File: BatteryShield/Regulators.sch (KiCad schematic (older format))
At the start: 14 parts

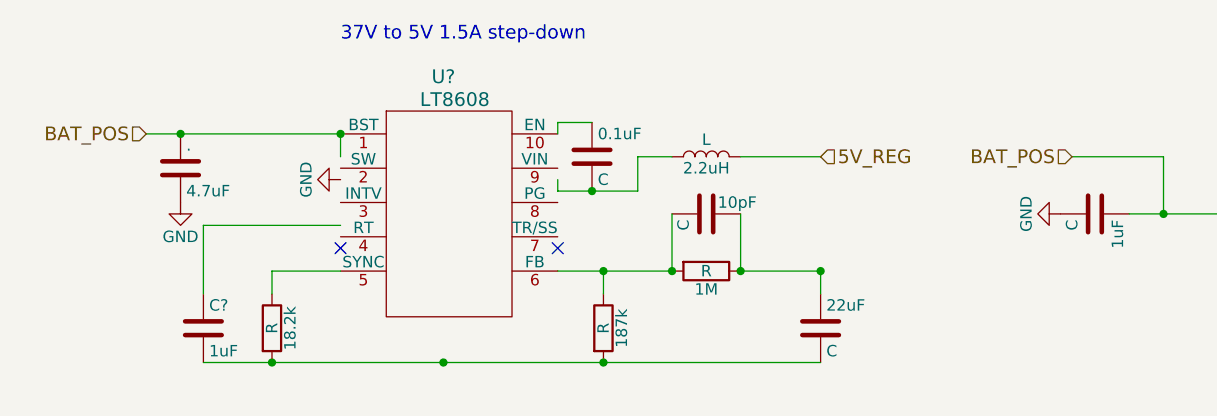
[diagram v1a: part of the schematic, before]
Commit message: Added two pages, cleaned up net names
Cleaned up net names. Added protection/grounding and BBB interface socket. Additional work needs to be done with grounding/mounting holes and 37V rail reverse current protection.
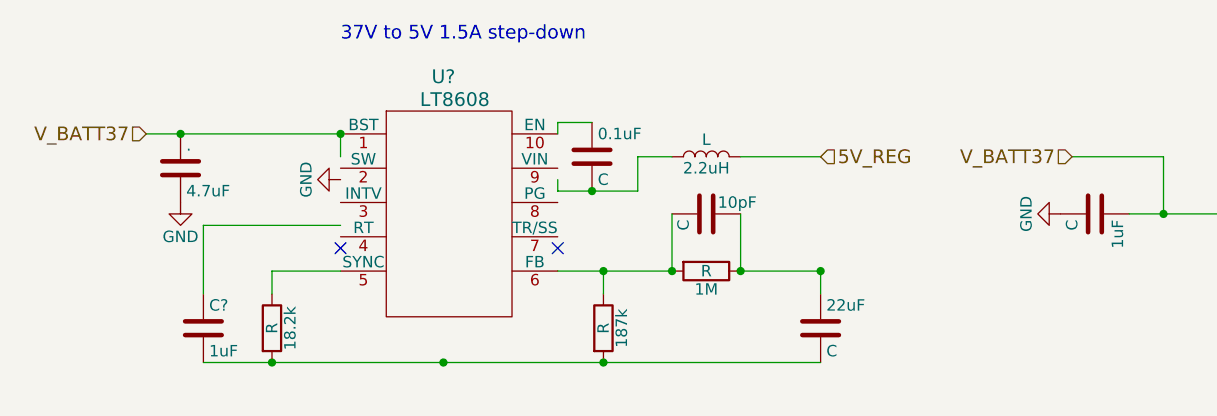
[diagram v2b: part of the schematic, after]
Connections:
- net labels added: V_BATT37
- net labels removed: BAT_POS
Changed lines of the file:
@@
 $Descr A4 11693 8268
 encoding utf-8
-Sheet 9 10
+Sheet 9 12
 Title ""
 Date ""
@@
 37V to 5V 1.5A step-down
 Text HLabel 1600 3050 0    60   Input ~ 0
-BAT_POS
+V_BATT37
 $Comp
 L C .
@@
 	5900 3400 6500 3400
 Text HLabel 5650 3150 0    60   Input ~ 0
-BAT_POS
+V_BATT37
 Wire Wire Line
 	5650 3150 6050 3150

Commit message: Associated a lot of footprints
Now I need to add a lot more :(
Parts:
- U?: footprint (none) -> footprints:MSOP10
- U?: footprint (none) -> footprints:MSOP8
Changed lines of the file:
@@
 $Descr A4 11693 8268
 encoding utf-8
-Sheet 9 12
+Sheet 12 12
 Title ""
 Date ""
@@
 F 0 "U?" H 2900 3900 60  0000 C CNN
 F 1 "LT8608" H 2950 3800 60  0000 C CNN
-F 2 "" H 2900 3350 60  0001 C CNN
-F 3 "" H 2900 3350 60  0001 C CNN
+F 2 "footprints:MSOP10" H 2900 3350 60  0001 C CNN
+F 3 "http://www.analog.com/media/en/technical-documentation/data-sheets/lt8608.pdf" H 2900 3350 60  0001 C CNN
 	1    2900 3350
 	1    0    0    -1
@@
 F 0 "U?" H 7000 3700 60  0000 C CNN
 F 1 "LTC3642-3.3" H 7000 3600 60  0000 C CNN
-F 2 "" H 6950 3350 60  0001 C CNN
-F 3 "" H 6950 3350 60  0001 C CNN
+F 2 "footprints:MSOP8" H 6950 3350 60  0001 C CNN
+F 3 "http://www.analog.com/media/en/technical-documentation/data-sheets/3642fc.pdf?domain=www.linear.com" H 6950 3350 60  0001 C CNN
 	1    6950 3350
 	1    0    0    -1

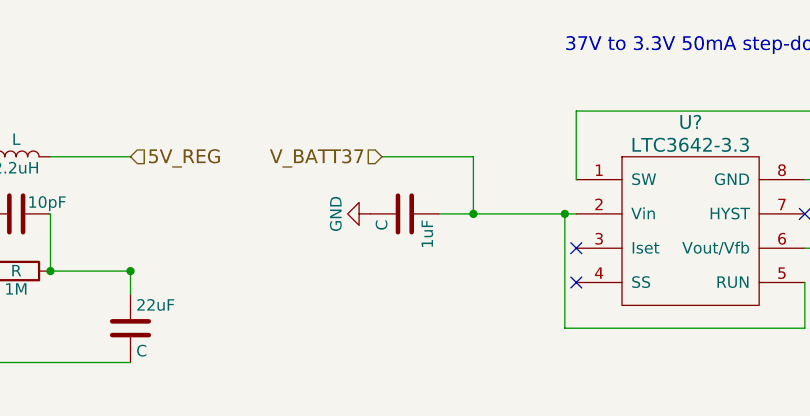
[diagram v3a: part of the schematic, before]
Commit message: Added more footprints
wow. much many foot prints
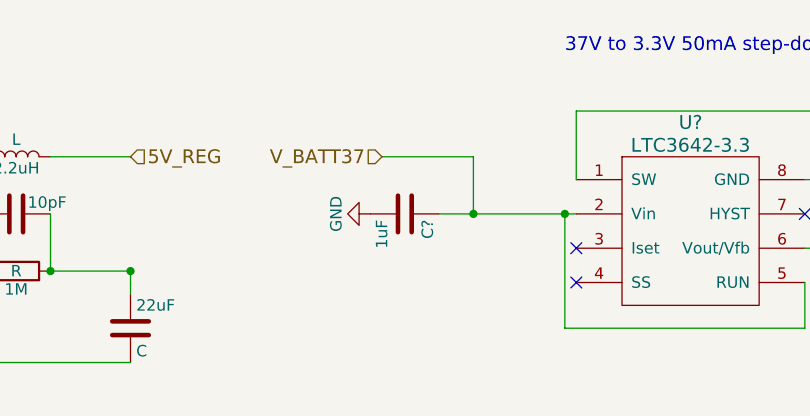
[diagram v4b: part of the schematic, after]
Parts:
- removed 1uF: C, symbol C
- added C?: 1uF, Capacitors_SMD:C_0603, symbol C
- ., 10pF, C?: footprint (none) -> Capacitors_SMD:C_0603
- 0.1uF: footprint (none) -> Capacitors_SMD:C_0402
- 10uF, 22uF: footprint (none) -> Capacitors_SMD:C_0805
- 150uH: footprint (none) -> Inductors_SMD:L_Wuerth_HCI-1350
- 18.2k: footprint (none) -> Resistors_SMD:R_0603
- 187k, 1M: footprint (none) -> Resistors_SMD:R_0805
- 2.2uH: footprint (none) -> Inductors_SMD:L_1812
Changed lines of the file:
@@
 F 0 "." H 1775 3300 50  0000 L CNN
 F 1 "4.7uF" H 1775 3100 50  0000 L CNN
-F 2 "" H 1788 3050 50  0001 C CNN
-F 3 "" H 1750 3200 50  0001 C CNN
+F 2 "Capacitors_SMD:C_0603" H 1788 3050 50  0001 C CNN
+F 3 "http://www.samsungsem.com/kr/support/product-search/mlcc/__icsFiles/afieldfile/2017/10/14/Spec%20sheet_CL10B475KQ8NQNC.pdf" H 1750 3200 50  0001 C CNN
 	1    1750 3200
 	1    0    0    -1
@@
 F 0 "C?" H 1875 4000 50  0000 L CNN
 F 1 "1uF" H 1875 3800 50  0000 L CNN
-F 2 "" H 1888 3750 50  0001 C CNN
-F 3 "" H 1850 3900 50  0001 C CNN
+F 2 "Capacitors_SMD:C_0603" H 1888 3750 50  0001 C CNN
+F 3 "http://www.samsungsem.com/kr/support/product-search/mlcc/__icsFiles/afieldfile/2017/07/27/Spec%20sheet_CL10B105MO8NNWC.pdf" H 1850 3900 50  0001 C CNN
 	1    1850 3900
 	1    0    0    -1
@@
 F 0 "18.2k" V 2230 3900 50  0000 C CNN
 F 1 "R" V 2150 3900 50  0000 C CNN
-F 2 "" V 2080 3900 50  0001 C CNN
-F 3 "" H 2150 3900 50  0001 C CNN
+F 2 "Resistors_SMD:R_0603" V 2080 3900 50  0001 C CNN
+F 3 "https://industrial.panasonic.com/cdbs/www-data/pdf/RDM0000/AOA0000C307.pdf" H 2150 3900 50  0001 C CNN
 	1    2150 3900
 	1    0    0    -1
@@
 F 0 "187k" V 3680 3900 50  0000 C CNN
 F 1 "R" V 3600 3900 50  0000 C CNN
-F 2 "" V 3530 3900 50  0001 C CNN
-F 3 "" H 3600 3900 50  0001 C CNN
+F 2 "Resistors_SMD:R_0805" V 3530 3900 50  0001 C CNN
+F 3 "https://www.digikey.ca/product-detail/en/panasonic-electronic-components/ERA-6AEB1873V/P187KDACT-ND/3075001" H 3600 3900 50  0001 C CNN
 	1    3600 3900
 	1    0    0    -1
@@
 F 0 "10pF" V 4000 3450 50  0000 L CNN
 F 1 "C" H 4075 3300 50  0000 L CNN
-F 2 "" H 4088 3250 50  0001 C CNN
-F 3 "" H 4050 3400 50  0001 C CNN
+F 2 "Capacitors_SMD:C_0603" H 4088 3250 50  0001 C CNN
+F 3 "https://www.murata.com/~/media/webrenewal/support/library/catalog/products/capacitor/mlcc/c02e.ashx" H 4050 3400 50  0001 C CNN
 	1    4050 3400
 	0    1    1    0
@@
 F 0 "1M" V 4130 3650 50  0000 C CNN
 F 1 "R" V 4050 3650 50  0000 C CNN
-F 2 "" V 3980 3650 50  0001 C CNN
-F 3 "" H 4050 3650 50  0001 C CNN
+F 2 "Resistors_SMD:R_0805" V 3980 3650 50  0001 C CNN
+F 3 "https://industrial.panasonic.com/cdbs/www-data/pdf/RDM0000/AOA0000C307.pdf" H 4050 3650 50  0001 C CNN
 	1    4050 3650
 	0    1    1    0
@@
 F 0 "22uF" H 4575 4000 50  0000 L CNN
 F 1 "C" H 4575 3800 50  0000 L CNN
-F 2 "" H 4588 3750 50  0001 C CNN
-F 3 "" H 4550 3900 50  0001 C CNN
+F 2 "Capacitors_SMD:C_0805" H 4588 3750 50  0001 C CNN
+F 3 "http://www.samsungsem.com/kr/support/product-search/mlcc/__icsFiles/afieldfile/2017/07/28/S_CL21A226MOCLRNC.pdf" H 4550 3900 50  0001 C CNN
 	1    4550 3900
 	1    0    0    -1
@@
 F 0 "0.1uF" H 3575 3250 50  0000 L CNN
 F 1 "C" H 3575 3050 50  0000 L CNN
-F 2 "" H 3588 3000 50  0001 C CNN
-F 3 "" H 3550 3150 50  0001 C CNN
+F 2 "Capacitors_SMD:C_0402" H 3588 3000 50  0001 C CNN
+F 3 "http://www.samsungsem.com/kr/support/product-search/mlcc/__icsFiles/afieldfile/2016/08/18/S_CL05F104ZO5NNNC.pdf" H 3550 3150 50  0001 C CNN
 	1    3550 3150
 	1    0    0    -1
@@
 F 0 "2.2uH" V 4000 3150 50  0000 C CNN
 F 1 "L" V 4125 3150 50  0000 C CNN
-F 2 "" H 4050 3150 50  0001 C CNN
-F 3 "" H 4050 3150 50  0001 C CNN
+F 2 "Inductors_SMD:L_1812" H 4050 3150 50  0001 C CNN
+F 3 "http://www.vishay.com/docs/34061/isc1812.pdf" H 4050 3150 50  0001 C CNN
 	1    4050 3150
 	0    -1   -1   0
@@
 	6050 3150 6050 3400
 Connection ~ 6450 3400
-$Comp
-L C 1uF
-U 1 1 5A920FC1
-P 5750 3400
-F 0 "1uF" H 5775 3500 50  0000 L CNN
-F 1 "C" H 5775 3300 50  0000 L CNN
-F 2 "" H 5788 3250 50  0001 C CNN
-F 3 "" H 5750 3400 50  0001 C CNN
-	1    5750 3400
-	0    1    1    0
-$EndComp
 Connection ~ 6050 3400
 $Comp
@@
 F 0 "150uH" V 8050 3250 50  0000 C CNN
 F 1 "L" V 8175 3250 50  0000 C CNN
-F 2 "" H 8100 3250 50  0001 C CNN
-F 3 "" H 8100 3250 50  0001 C CNN
+F 2 "Inductors_SMD:L_Wuerth_HCI-1350" H 8100 3250 50  0001 C CNN
+F 3 "http://katalog.we-online.de/pbs/datasheet/7447709151.pdf" H 8100 3250 50  0001 C CNN
 	1    8100 3250
 	1    0    0    -1
@@
 F 0 "10uF" H 8275 3950 50  0000 L CNN
 F 1 "C" H 8275 3750 50  0000 L CNN
-F 2 "" H 8288 3700 50  0001 C CNN
-F 3 "" H 8250 3850 50  0001 C CNN
+F 2 "Capacitors_SMD:C_0805" H 8288 3700 50  0001 C CNN
+F 3 "http://www.samsungsem.com/kr/support/product-search/mlcc/CL21A106KPCLQNC.jsp" H 8250 3850 50  0001 C CNN
 	1    8250 3850
 	1    0    0    -1
@@
 	1    0    0    -1
 $EndComp
+$Comp
+L C C?
+U 1 1 5B29BC47
+P 5750 3400
+F 0 "C?" H 5775 3500 50  0000 L CNN
+F 1 "1uF" H 5775 3300 50  0000 L CNN
+F 2 "Capacitors_SMD:C_0603" H 5788 3250 50  0001 C CNN
+F 3 "http://www.samsungsem.com/kr/support/product-search/mlcc/__icsFiles/afieldfile/2017/07/27/Spec%20sheet_CL10B105MO8NNWC.pdf" H 5750 3400 50  0001 C CNN
+	1    5750 3400
+	0    1    1    0
+$EndComp
 $EndSCHEMATC

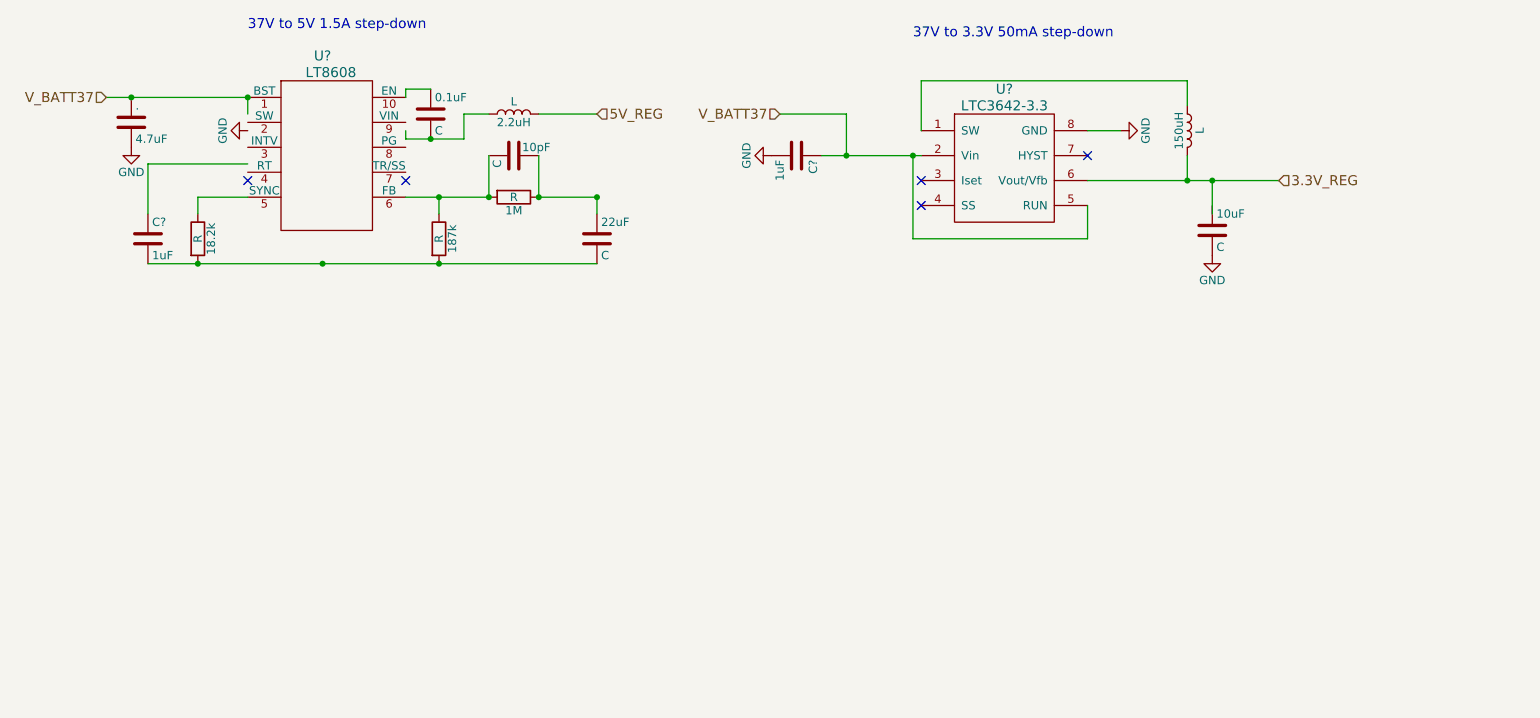
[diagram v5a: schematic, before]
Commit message: Did V.1 of layout; removed old circuits
gosh I need to do schoolwork
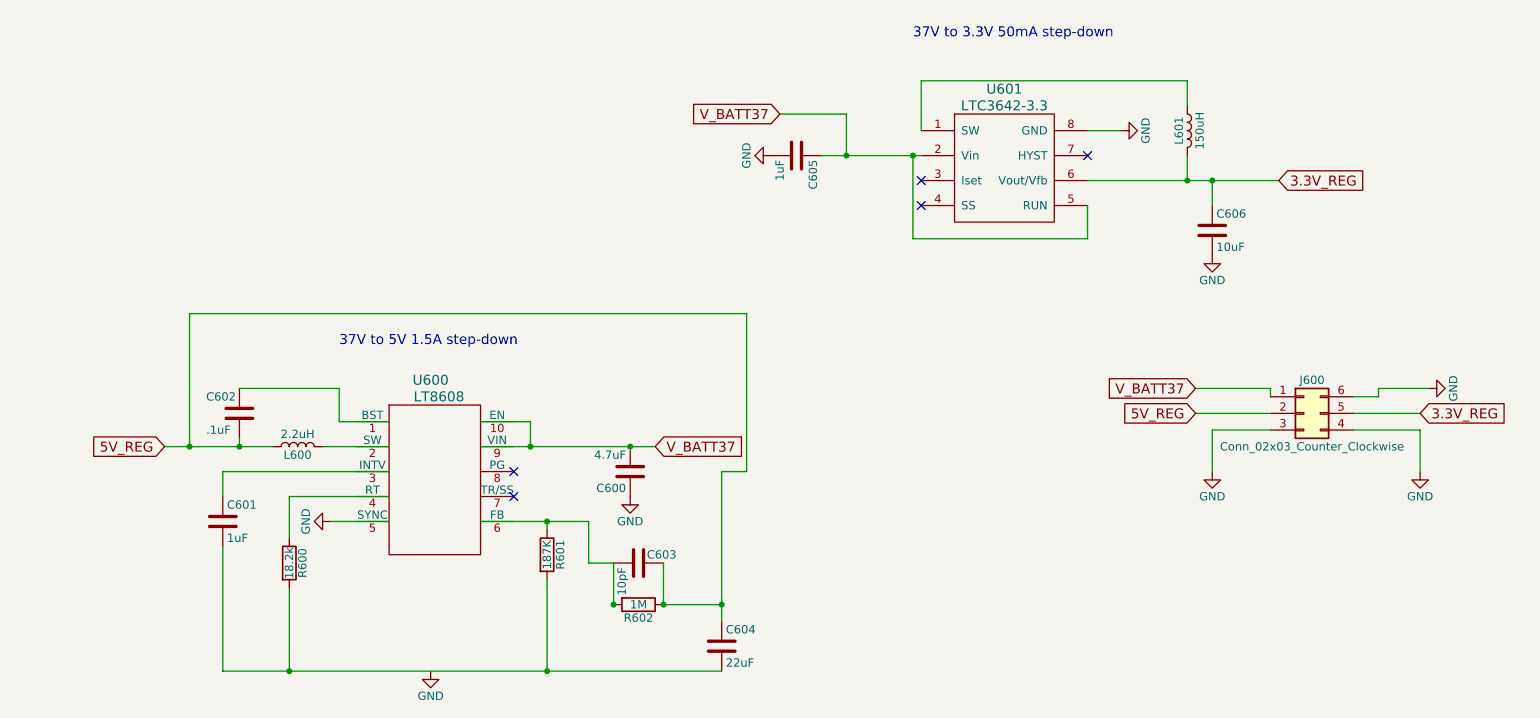
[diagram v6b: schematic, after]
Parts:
- added J600: Conn_02x03_Counter_Clockwise, Connectors_Molex:Molex_MiniFit-JR-5556-06B_2x03x4.20mm_Straight, symbol Conn_02x03_Counter_Clockwise
- C602: renamed from 0.1uF; value C -> .1uF
- C603: renamed from 10pF; value C -> 10pF
- C604: renamed from 22uF; value C -> 22uF
- C606: renamed from 10uF; value C -> 10uF
- L600: renamed from 2.2uH; value L -> 2.2uH
- L601: renamed from 150uH; value L -> 150uH
- R600: renamed from 18.2k; value R -> 18.2k
- R601: renamed from 187k; value R -> 187K
- R602: renamed from 1M; value R -> 1M
- gave numbers to parts that had none: 4
- renumbered . to C600
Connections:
- wire segments 33 -> 54
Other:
- moved on the sheet: C600, C601, C602, C603, C604, L600, R600, R601, R602, U600
